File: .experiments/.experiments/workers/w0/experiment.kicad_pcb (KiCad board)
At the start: 2 copper layers, 140 x 90 mm, 39 parts, among them J1 USB_C, J2 Output, J3 Debug, Q1 FS8205A, U1 USBLC6-2SC6, U2 BQ24072, U3 HY2113-KB5B, U4 MT3608, U5 AP2112K-3.3, U6 LN61CN3302MR-G

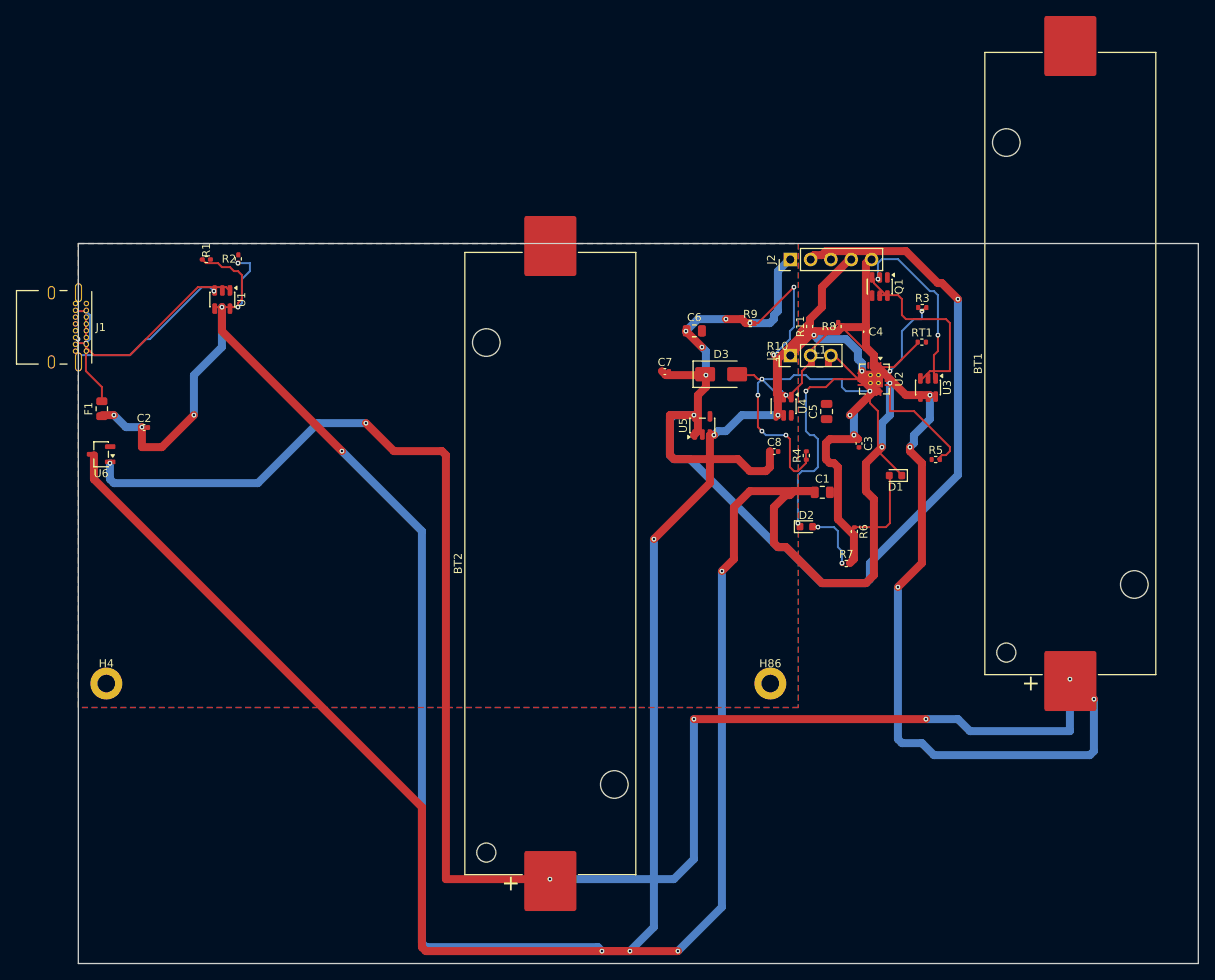
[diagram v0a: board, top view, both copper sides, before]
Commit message: Set uniform 6mil trace width (0.1524mm) for signal+power to reduce shorts
Baseline with 6mil: score=20.05 shorts=72 (vs 25.66@82shorts before)
Round 1: 20.45 shorts=93
Round 2: 20.65 shorts=84 [NEW BEST]
Round 3: 19.44 shorts=72

Trading off routing flexibility for cleaner DRC (no catastrophic shorts).
Tighter routing but more predictable.

Co-Authored-By: Claude Opus 4.6 <noreply@anthropic.com>
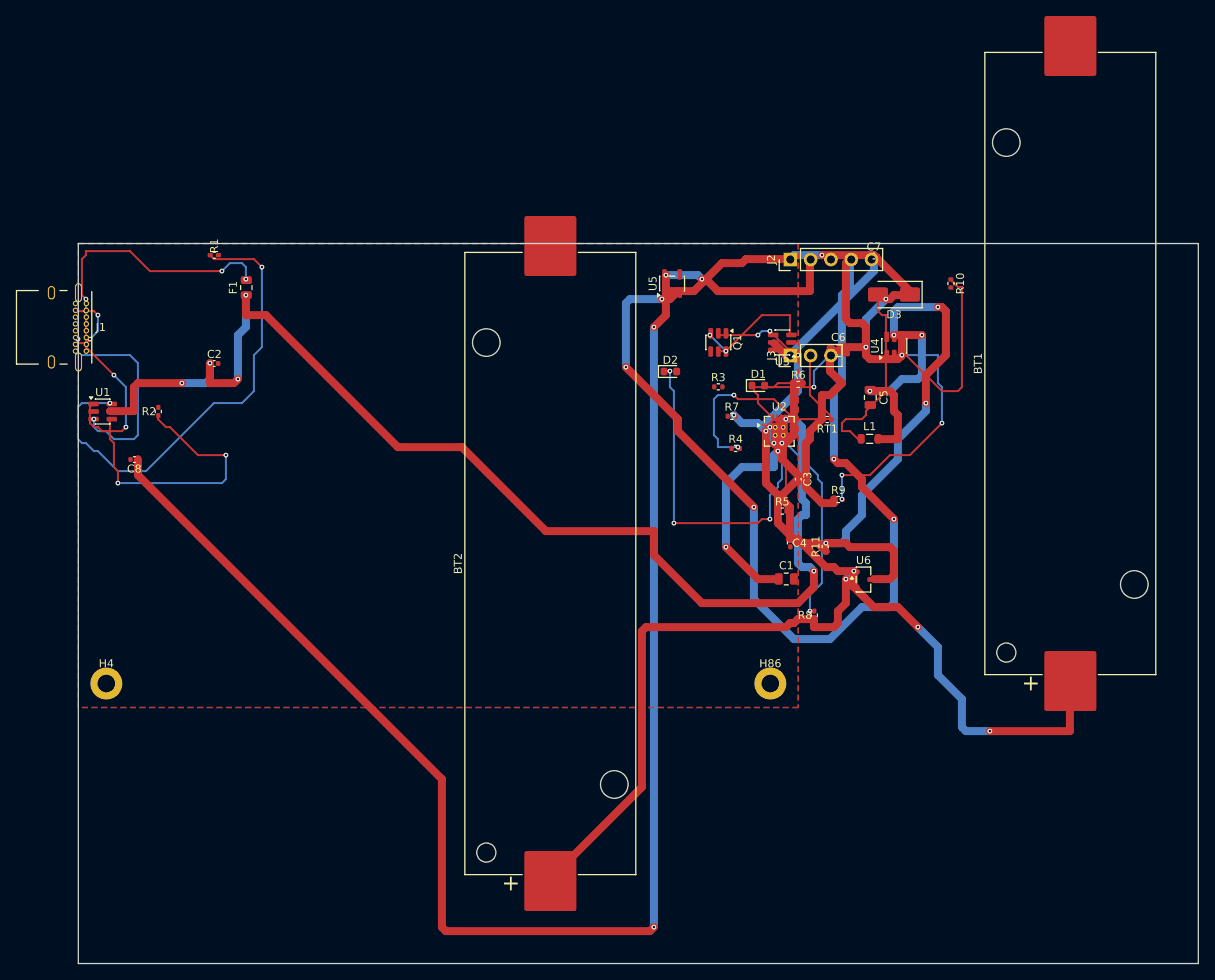
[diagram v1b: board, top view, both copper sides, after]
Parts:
- moved U6 96.6 mm to (98.1, 42.0), turned to 0 degrees
- moved C8 80.0 mm to (7.00, 27.0), turned to 180 degrees
- moved R8 36.2 mm to (92.0, 46.5)
- moved C7 29.8 mm to (99.4, 1.57)
- moved C4 28.1 mm to (89.0, 37.4)
- moved R11 27.6 mm to (93.4, 37.9)
- moved R3 27.4 mm to (80.0, 17.9)
- moved D2 25.8 mm to (74.0, 16.0)
- moved R9 24.6 mm to (95.0, 32.0)
- moved D3 23.8 mm to (102.0, 6.38), turned to 180 degrees
- moved F1 23.6 mm to (21.0, 5.51)
- moved R10 23.5 mm to (109.1, 5.00), turned to -90 degrees
- moved R7 23.3 mm to (81.7, 21.6)
- moved R2 21.5 mm to (10.0, 21.0)
- moved Q1 21.4 mm to (80.0, 12.4)
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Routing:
- net /VBAT: track 321.1 -> 172.5 mm, vias 10 -> 8
- net /VBUS: track 273.7 -> 180.7 mm, vias 10 -> 8
- net /3V3: track 124.0 -> 206.1 mm, vias 2 -> 4
- net Net-(R1-Pad1): track 11.0 -> 59.0 mm, vias 0 -> 2
- net /5V: track 40.7 -> 74.6 mm, vias 6 -> 4
- net Net-(U4-FB): track 22.1 -> 55.4 mm, vias 2 -> 4
- net /VSYS_BOOST: track 0.00 -> 27.2 mm, vias 0 -> 2
- net /NTC_SENSE: track 19.0 -> 45.1 mm, vias 0 -> 2
- net Net-(R2-Pad1): track 10.6 -> 36.0 mm
- net Net-(F1-Pad2): track 14.7 -> 38.9 mm, vias 2 -> 6
- net Net-(D2-K): track 27.9 -> 42.0 mm, vias 2 -> 4
- net Net-(U2-ILIM): track 35.1 -> 21.2 mm, vias 4 -> 2
- net Net-(Q1A-G): track 22.3 -> 10.2 mm
- net Net-(D3-A): track 13.3 -> 24.1 mm, vias 2 -> 0
- net Net-(U2-ISET): track 10.4 -> 0.00 mm, vias 2 -> 0
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
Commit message: Hard-block cross-net traces to eliminate shorts (50% of DRC failures)
Critical fixes:
- Mark routed traces/vias at 1e6 (hard block) in solve() instead of 100 (soft)
- A* now cannot cross completed nets → no more shorting through existing traces
- Mark escape vias on grid immediately (was invisible, caused via collisions)
- Add clearance margin to via markings (0.5mm approach distance enforced)
- Raise max_search to 2M (hard blocks require longer detours)
- Wire max_search config through __init__ and all find_path calls

Test added: test_hard_block_prevents_cross_net_routing verifies blocked cells
are uncrossable, forcing detours instead.

Expected impact: DRC shorts should drop from ~80 to near-zero.

Co-Authored-By: Claude Opus 4.6 <noreply@anthropic.com>
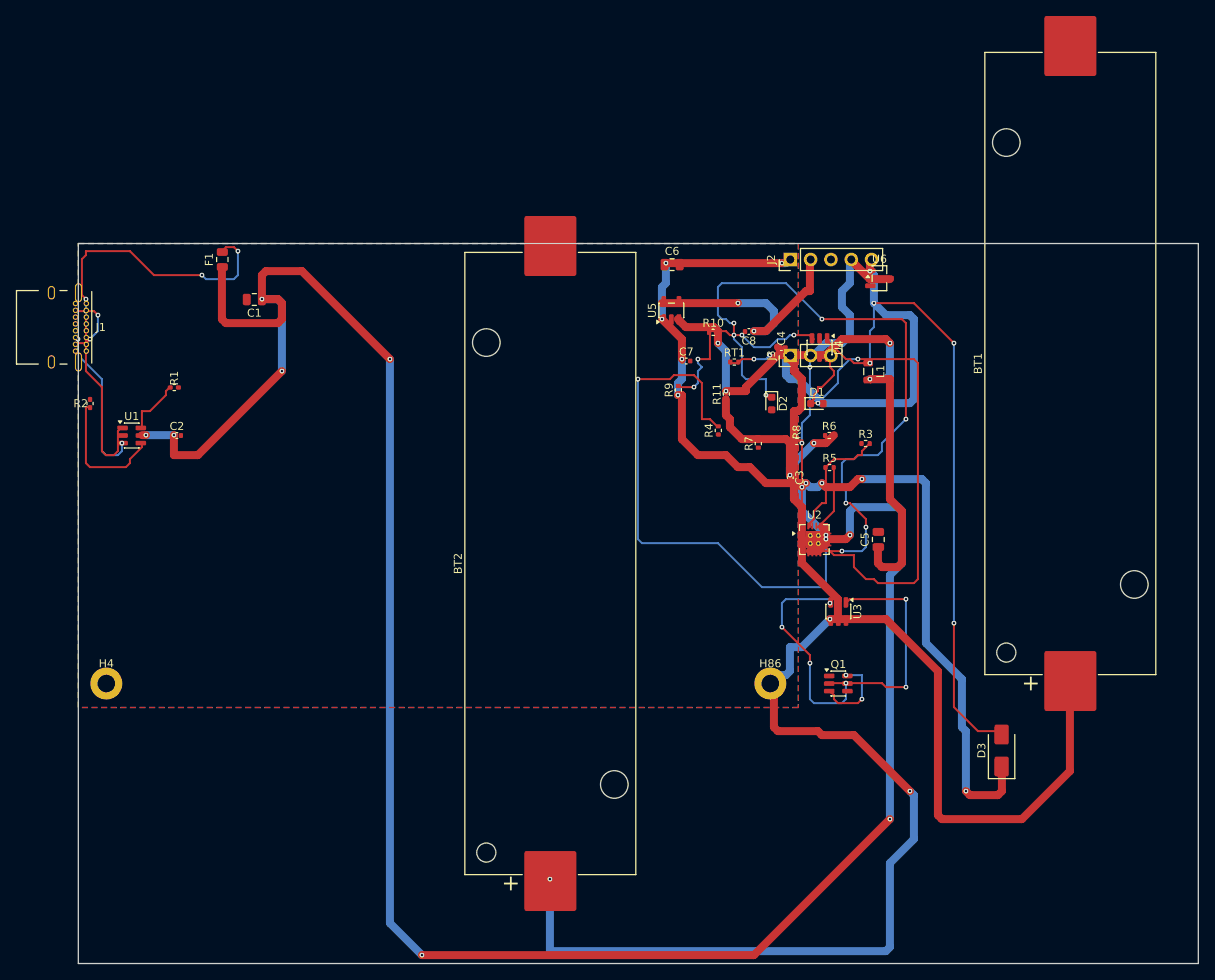
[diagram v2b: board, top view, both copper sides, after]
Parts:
- moved C8 78.5 mm to (83.8, 11.0)
- moved C1 75.1 mm to (22.0, 7.00), turned to 180 degrees
- moved D3 58.6 mm to (115.4, 63.4), turned to 90 degrees
- moved Q1 45.2 mm to (95.0, 55.0), turned to 0 degrees
- moved U6 37.7 mm to (100.1, 4.34)
- moved U3 34.4 mm to (95.0, 46.0), turned to -90 degrees
- moved R10 30.3 mm to (79.4, 11.1), turned to 0 degrees
- moved C7 26.9 mm to (76.0, 14.7)
- moved C4 24.5 mm to (87.9, 13.0), turned to 0 degrees
- moved R9 24.2 mm to (75.0, 18.3), turned to 90 degrees
- moved C6 23.4 mm to (74.2, 2.64)
- moved R11 22.7 mm to (81.0, 18.8)
- moved R8 21.8 mm to (89.8, 24.7), turned to 0 degrees
- moved R3 19.7 mm to (98.4, 25.0)
- moved C5 17.8 mm to (100.0, 37.0), turned to 90 degrees
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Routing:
- net /3V3: track 206.1 -> 31.9 mm, vias 4 -> 2
- net /EN: track 203.2 -> 48.9 mm, vias 10 -> 4
- net /VBUS: track 180.7 -> 274.4 mm
- net /VBAT: track 172.5 -> 256.4 mm, vias 8 -> 6
- net Net-(D3-A): track 24.1 -> 79.5 mm, vias 0 -> 4
- net Net-(R1-Pad1): track 59.0 -> 7.04 mm, vias 2 -> 0
- net /5V: track 74.6 -> 122.2 mm, vias 4 -> 11
- net Net-(U2-ILIM): track 21.2 -> 67.7 mm
- net /CHG_N: track 20.9 -> 66.1 mm, vias 2 -> 3
- net Net-(D2-K): track 42.0 -> 85.6 mm, vias 4 -> 8
- net Net-(U4-FB): track 55.4 -> 25.8 mm
- net /VSYS_BOOST: track 27.2 -> 48.3 mm
- net Net-(R2-Pad1): track 36.0 -> 16.5 mm, vias 2 -> 0
- net Net-(Q1A-G): track 10.2 -> 28.4 mm
- net Net-(U2-ISET): track 0.00 -> 15.7 mm
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
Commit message: Clean up: remove 50M+ of old experiment artifacts
Removed:
- .tmp_router_regression/ (11M baseline)
- .experiments/workers/ (40M+ old copies)
- .experiments/frames/ (old snapshots)

Kept: latest PCB, GIF, config, results

Co-Authored-By: Claude Opus 4.6 <noreply@anthropic.com>
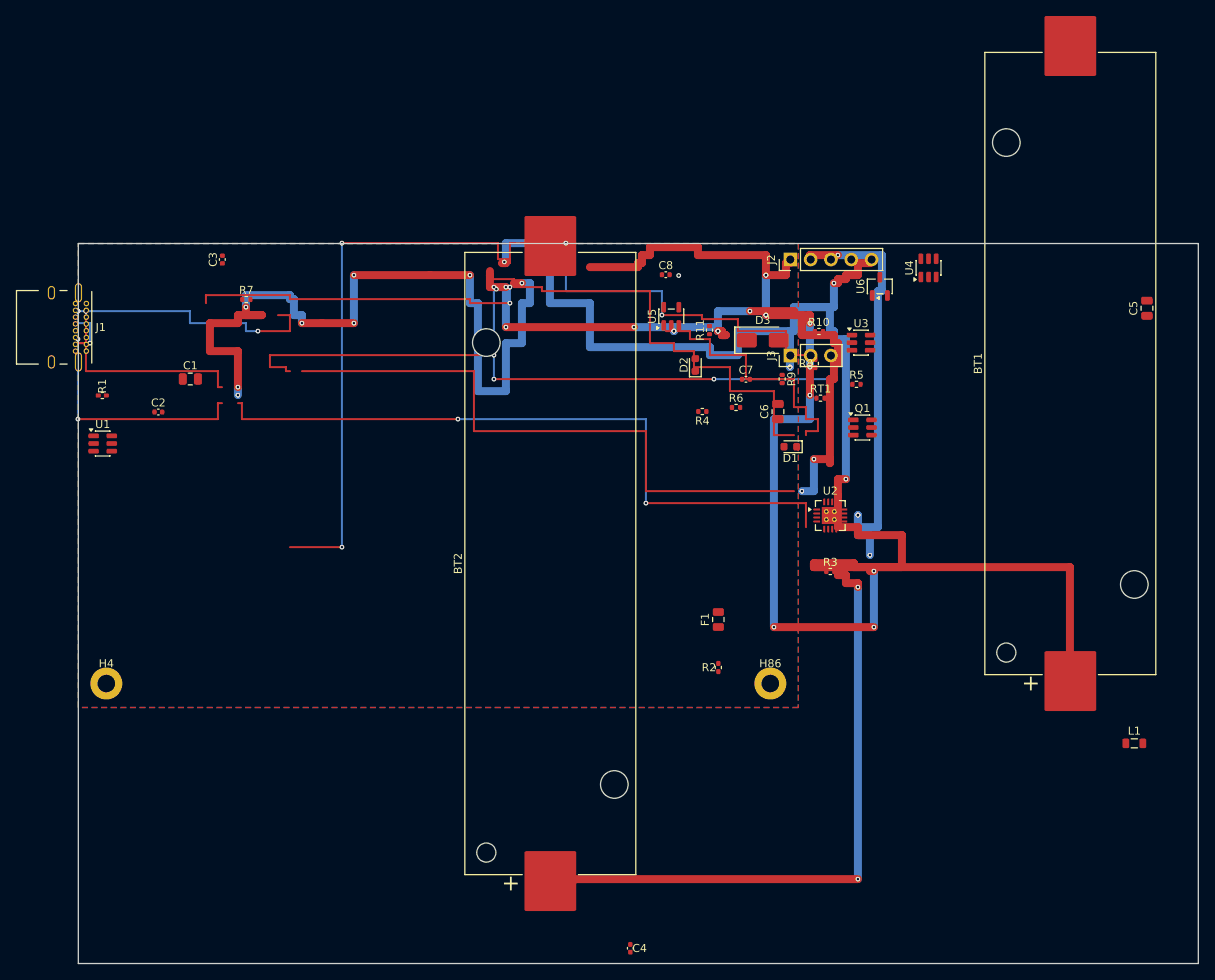
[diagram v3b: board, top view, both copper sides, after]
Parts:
- moved R2 85.2 mm to (80.0, 53.0)
- moved C4 77.4 mm to (69.0, 88.1), turned to -90 degrees
- moved F1 76.6 mm to (80.0, 47.0)
- moved C3 76.1 mm to (18.0, 2.00), turned to 90 degrees
- moved R7 66.5 mm to (21.0, 7.00), turned to 0 degrees
- moved D3 59.3 mm to (85.6, 12.1), turned to 0 degrees
- moved L1 57.2 mm to (132.0, 62.5), turned to 0 degrees
- moved C5 44.3 mm to (133.6, 8.09)
- moved U3 33.7 mm to (97.8, 12.4), turned to 0 degrees
- moved Q1 32.1 mm to (98.0, 23.0)
- moved C6 22.6 mm to (87.5, 21.0), turned to 90 degrees
- moved U4 16.9 mm to (106.3, 3.04), turned to 90 degrees
- moved R3 16.6 mm to (94.0, 41.0)
- moved R10 13.2 mm to (92.6, 11.0)
- moved R9 13.1 mm to (88.0, 16.9), turned to -90 degrees
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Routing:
- net /VBUS: track 274.4 -> 99.5 mm
- net /NTC_SENSE: track 33.3 -> 123.0 mm
- net Net-(D3-A): track 79.5 -> 0.00 mm, vias 4 -> 0
- net Net-(D1-A): track 0.00 -> 76.5 mm
- net Net-(R2-Pad1): track 16.5 -> 86.5 mm, vias 0 -> 2
- net /EN: track 48.9 -> 0.00 mm, vias 4 -> 0
- net /VSYS: track 37.0 -> 85.5 mm, vias 4 -> 10
- net /VSYS_BOOST: track 48.3 -> 0.00 mm, vias 2 -> 0
- net Net-(D2-A): track 0.00 -> 33.5 mm
- net /CHG_N: track 66.1 -> 99.5 mm, vias 3 -> 6
- net Net-(Q1A-G): track 28.4 -> 0.00 mm, vias 2 -> 0
- net Net-(D2-K): track 85.6 -> 57.5 mm, vias 8 -> 0
- net Net-(Q1B-G): track 27.1 -> 0.00 mm, vias 4 -> 0
- net Net-(U4-FB): track 25.8 -> 0.00 mm, vias 4 -> 0
- net Net-(U2-ILIM): track 67.7 -> 42.0 mm
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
